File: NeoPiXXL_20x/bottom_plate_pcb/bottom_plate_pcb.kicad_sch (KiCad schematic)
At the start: 10 parts, among them J1 Leg, J2 Leg, J3 Leg, J4 Leg

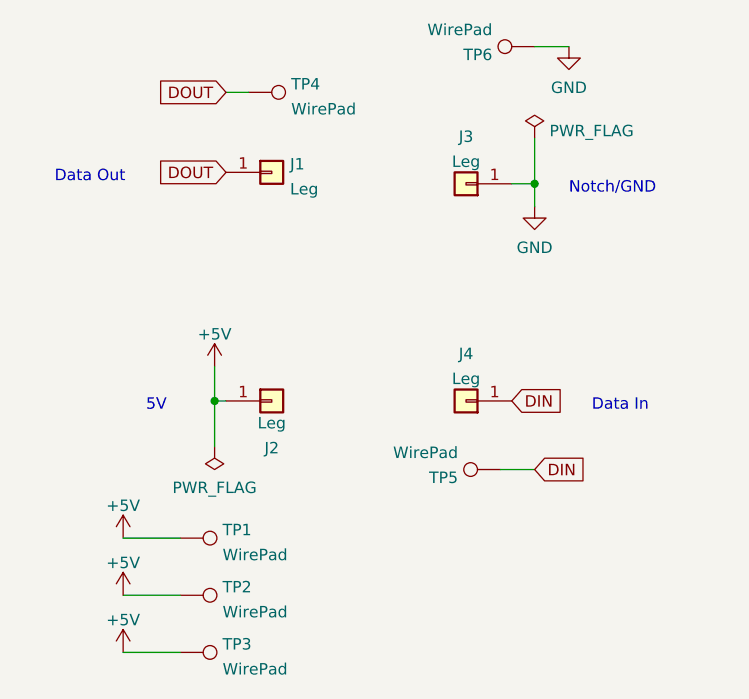
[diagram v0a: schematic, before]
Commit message: fixed DOUT/DIN swap for 20x variant
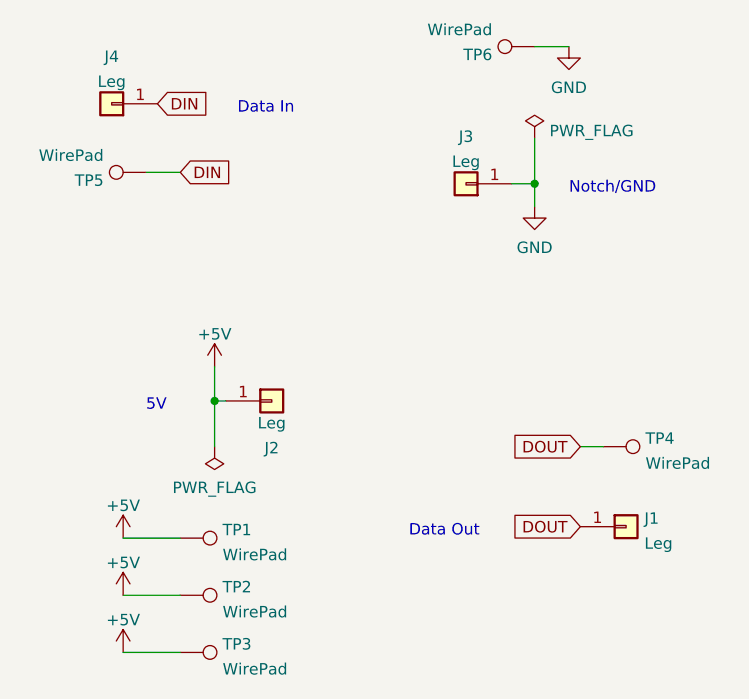
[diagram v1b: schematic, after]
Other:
- moved on the sheet: J1, J4, TP4, TP5
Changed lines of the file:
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@@
   (junction (at 74.93 99.06) (diameter 0) (color 0 0 0 0)
   )
-  (wire (pts (xy 76.2 64.77) (xy 78.74 64.77))
+  (wire (pts (xy 115.57 104.14) (xy 118.11 104.14))
     (stroke (width 0) (type default) (color 0 0 0 0))
   )
@@
     (stroke (width 0) (type default) (color 0 0 0 0))
   )
-  (wire (pts (xy 110.49 106.68) (xy 106.68 106.68))
+  (wire (pts (xy 71.12 73.66) (xy 67.31 73.66))
     (stroke (width 0) (type default) (color 0 0 0 0))
   )
@@
     (effects (font (size 1.27 1.27)) (justify left bottom))
   )
-  (text "Data In" (at 116.84 100.33 0)
+  (text "Data In" (at 77.47 67.31 0)
     (effects (font (size 1.27 1.27)) (justify left bottom))
   )
-  (text "Data Out" (at 57.15 74.93 0)
+  (text "Data Out" (at 96.52 114.3 0)
     (effects (font (size 1.27 1.27)) (justify left bottom))
   )
@@
     (effects (font (size 1.27 1.27)) (justify left bottom))
   )
-  (global_label "DOUT" (shape input) (at 76.2 73.66 180) (fields_autoplaced)
+  (global_label "DOUT" (shape input) (at 115.57 113.03 180) (fields_autoplaced)
     (effects (font (size 1.27 1.27)) (justify right))
-    (property "Intersheet References" "${INTERSHEET_REFS}" (id 0) (at 68.8883 73.7394 0)
+    (property "Intersheet References" "${INTERSHEET_REFS}" (id 0) (at 108.2583 113.1094 0)
       (effects (font (size 1.27 1.27)) (justify right) hide)
     )
   )
-  (global_label "DIN" (shape input) (at 110.49 106.68 0) (fields_autoplaced)
+  (global_label "DIN" (shape input) (at 71.12 73.66 0) (fields_autoplaced)
     (effects (font (size 1.27 1.27)) (justify left))
-    (property "Intersheet References" "${INTERSHEET_REFS}" (id 0) (at 116.1083 106.6006 0)
+    (property "Intersheet References" "${INTERSHEET_REFS}" (id 0) (at 76.7383 73.5806 0)
       (effects (font (size 1.27 1.27)) (justify left) hide)
     )
   )
-  (global_label "DOUT" (shape input) (at 76.2 64.77 180) (fields_autoplaced)
+  (global_label "DOUT" (shape input) (at 115.57 104.14 180) (fields_autoplaced)
     (effects (font (size 1.27 1.27)) (justify right))
-    (property "Intersheet References" "${INTERSHEET_REFS}" (id 0) (at 68.8883 64.8494 0)
+    (property "Intersheet References" "${INTERSHEET_REFS}" (id 0) (at 108.2583 104.2194 0)
       (effects (font (size 1.27 1.27)) (justify right) hide)
     )
   )
-  (global_label "DIN" (shape input) (at 107.95 99.06 0) (fields_autoplaced)
+  (global_label "DIN" (shape input) (at 68.58 66.04 0) (fields_autoplaced)
     (effects (font (size 1.27 1.27)) (justify left))
-    (property "Intersheet References" "${INTERSHEET_REFS}" (id 0) (at 113.5683 98.9806 0)
+    (property "Intersheet References" "${INTERSHEET_REFS}" (id 0) (at 74.1983 65.9606 0)
       (effects (font (size 1.27 1.27)) (justify left) hide)
     )
@@
     (pin "1")
   )
-  (symbol (lib_id "Connector_Generic:Conn_01x01") (at 102.87 99.06 180) (unit 1)
-    (in_bom yes) (on_board yes) (fields_autoplaced)
-    (property "Reference" "J4" (id 0) (at 102.87 93.8235 0))
-    (property "Value" "Leg" (id 1) (at 102.87 96.5986 0))
-    (property "Footprint" "prints:pin_pad" (id 2) (at 102.87 99.06 0)
-      (effects (font (size 1.27 1.27)) hide)
-    )
-    (property "Datasheet" "~" (id 3) (at 102.87 99.06 0)
+  (symbol (lib_id "Connector_Generic:Conn_01x01") (at 63.5 66.04 180) (unit 1)
+    (in_bom yes) (on_board yes) (fields_autoplaced)
+    (property "Reference" "J4" (id 0) (at 63.5 60.8035 0))
+    (property "Value" "Leg" (id 1) (at 63.5 63.5786 0))
+    (property "Footprint" "prints:pin_pad" (id 2) (at 63.5 66.04 0)
+      (effects (font (size 1.27 1.27)) hide)
+    )
+    (property "Datasheet" "~" (id 3) (at 63.5 66.04 0)
       (effects (font (size 1.27 1.27)) hide)
     )
@@
     (pin "1")
   )
-  (symbol (lib_id "Connector:TestPoint") (at 78.74 64.77 270) (unit 1)
-    (in_bom yes) (on_board yes) (fields_autoplaced)
-    (property "Reference" "TP4" (id 0) (at 83.439 63.8615 90)
-      (effects (font (size 1.27 1.27)) (justify left))
-    )
-    (property "Value" "WirePad" (id 1) (at 83.439 66.6366 90)
-      (effects (font (size 1.27 1.27)) (justify left))
-    )
-    (property "Footprint" "prints:WirePad" (id 2) (at 78.74 69.85 0)
-      (effects (font (size 1.27 1.27)) hide)
-    )
-    (property "Datasheet" "~" (id 3) (at 78.74 69.85 0)
-      (effects (font (size 1.27 1.27)) hide)
-    )
-    (pin "1")
-  )
-  (symbol (lib_id "Connector_Generic:Conn_01x01") (at 81.28 73.66 0) (unit 1)
-    (in_bom yes) (on_board yes) (fields_autoplaced)
-    (property "Reference" "J1" (id 0) (at 83.312 72.7515 0)
-      (effects (font (size 1.27 1.27)) (justify left))
-    )
-    (property "Value" "Leg" (id 1) (at 83.312 75.5266 0)
-      (effects (font (size 1.27 1.27)) (justify left))
-    )
-    (property "Footprint" "prints:pin_pad" (id 2) (at 81.28 73.66 0)
-      (effects (font (size 1.27 1.27)) hide)
-    )
-    (property "Datasheet" "~" (id 3) (at 81.28 73.66 0)
+  (symbol (lib_id "Connector:TestPoint") (at 118.11 104.14 270) (unit 1)
+    (in_bom yes) (on_board yes) (fields_autoplaced)
+    (property "Reference" "TP4" (id 0) (at 122.809 103.2315 90)
+      (effects (font (size 1.27 1.27)) (justify left))
+    )
+    (property "Value" "WirePad" (id 1) (at 122.809 106.0066 90)
+      (effects (font (size 1.27 1.27)) (justify left))
+    )
+    (property "Footprint" "prints:WirePad" (id 2) (at 118.11 109.22 0)
+      (effects (font (size 1.27 1.27)) hide)
+    )
+    (property "Datasheet" "~" (id 3) (at 118.11 109.22 0)
+      (effects (font (size 1.27 1.27)) hide)
+    )
+    (pin "1")
+  )
+  (symbol (lib_id "Connector_Generic:Conn_01x01") (at 120.65 113.03 0) (unit 1)
+    (in_bom yes) (on_board yes) (fields_autoplaced)
+    (property "Reference" "J1" (id 0) (at 122.682 112.1215 0)
+      (effects (font (size 1.27 1.27)) (justify left))
+    )
+    (property "Value" "Leg" (id 1) (at 122.682 114.8966 0)
+      (effects (font (size 1.27 1.27)) (justify left))
+    )
+    (property "Footprint" "prints:pin_pad" (id 2) (at 120.65 113.03 0)
+      (effects (font (size 1.27 1.27)) hide)
+    )
+    (property "Datasheet" "~" (id 3) (at 120.65 113.03 0)
       (effects (font (size 1.27 1.27)) hide)
     )
@@
     (pin "1")
   )
-  (symbol (lib_id "Connector:TestPoint") (at 106.68 106.68 90) (unit 1)
-    (in_bom yes) (on_board yes) (fields_autoplaced)
-    (property "Reference" "TP5" (id 0) (at 101.981 107.5885 90)
-      (effects (font (size 1.27 1.27)) (justify left))
-    )
-    (property "Value" "WirePad" (id 1) (at 101.981 104.8134 90)
-      (effects (font (size 1.27 1.27)) (justify left))
-    )
-    (property "Footprint" "prints:WirePad" (id 2) (at 106.68 101.6 0)
-      (effects (font (size 1.27 1.27)) hide)
-    )
-    (property "Datasheet" "~" (id 3) (at 106.68 101.6 0)
-      (effects (font (size 1.27 1.27)) hide)
-    )
+  (symbol (lib_id "Connector:TestPoint") (at 67.31 73.66 90) (unit 1)
+    (in_bom yes) (on_board yes) (fields_autoplaced)
+    (property "Reference" "TP5" (id 0) (at 62.611 74.5685 90)
+      (effects (font (size 1.27 1.27)) (justify left))
+    )
+    (property "Value" "WirePad" (id 1) (at 62.611 71.7934 90)
+      (effects (font (size 1.27 1.27)) (justify left))
+    )
+    (property "Footprint" "prints:WirePad" (id 2) (at 67.31 68.58 0)
+      (effects (font (size 1.27 1.27)) hide)
+    )
+    (property "Datasheet" "~" (id 3) (at 67.31 68.58 0)
+      (effects (font (size 1.27 1.27)) hide)
+    )
